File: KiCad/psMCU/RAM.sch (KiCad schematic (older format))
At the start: 26 parts

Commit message: Started work on schematic
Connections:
- net LATCHSAFEDA_EN/VAL renamed LED: LATCHSAFEDA_EN/VAL
- net R_ASYNC_SAFEA/VAL renamed LED: R_ASYNC_SAFEA/VAL
- net W_ASYNC/VAL renamed LED: W_ASYNC/VAL
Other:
- note added: "Latch Async Write.\nShould keep writes stable and \nprevent accidental writes."
- note added: "Only Do Something if RAM (0x000-0x0ff) and\nnot Periphs (0x100-0x1ff) are addressed."
- note removed: "Ensure Data is stabil during Write"
- note removed: "Only Do Something if RAM and\nnot Periphs are addressed."
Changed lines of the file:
@@
 $Descr A4 11693 8268
 encoding utf-8
-Sheet 51 65
+Sheet 21 94
 Title ""
 Date ""
@@
 Text HLabel 1050 1300 0    50   3State ~ 0
 DB[0..7]
-Text HLabel 1050 1650 0    50   Input ~ 0
+Text HLabel 1050 1650 0    50   BiDi ~ 0
 RAMA[0..8]
 Entry Wire Line
@@
 	1600 5900 1850 5900
 Text Notes 1550 6650 0    50   ~ 0
-Only Do Something if RAM and\nnot Periphs are addressed.
+Only Do Something if RAM (0x000-0x0ff) and\nnot Periphs (0x100-0x1ff) are addressed.
 Wire Bus Line
 	1950 1400 3800 1400
@@
 Wire Wire Line
 	4800 3000 4750 3000
-Text Notes 3950 3850 0    50   ~ 0
-Ensure Data is stabil during Write
+Text Notes 5050 4600 0    50   ~ 0
+Latch Async Write.\nShould keep writes stable and \nprevent accidental writes.
 Connection ~ 2750 3150
 Wire Wire Line
@@
 S 3100 5550 700  200
 U 5F31E1C9
-F0 "R_ASYNC_SAFEA" 50
+F0 "LED: R_ASYNC_SAFEA" 50
 F1 "1BitLED.sch" 50
 F2 "VAL" I L 3100 5650 50
@@
 S 3100 4650 700  200
 U 5F3261C9
-F0 "W_ASYNC" 50
+F0 "LED: W_ASYNC" 50
 F1 "1BitLED.sch" 50
 F2 "VAL" I L 3100 4750 50
@@
 S 3100 4050 700  200
 U 5F32E5C9
-F0 "LATCHSAFEDA_EN" 50
+F0 "LED: LATCHSAFEDA_EN" 50
 F1 "1BitLED.sch" 50
 F2 "VAL" I L 3100 4150 50

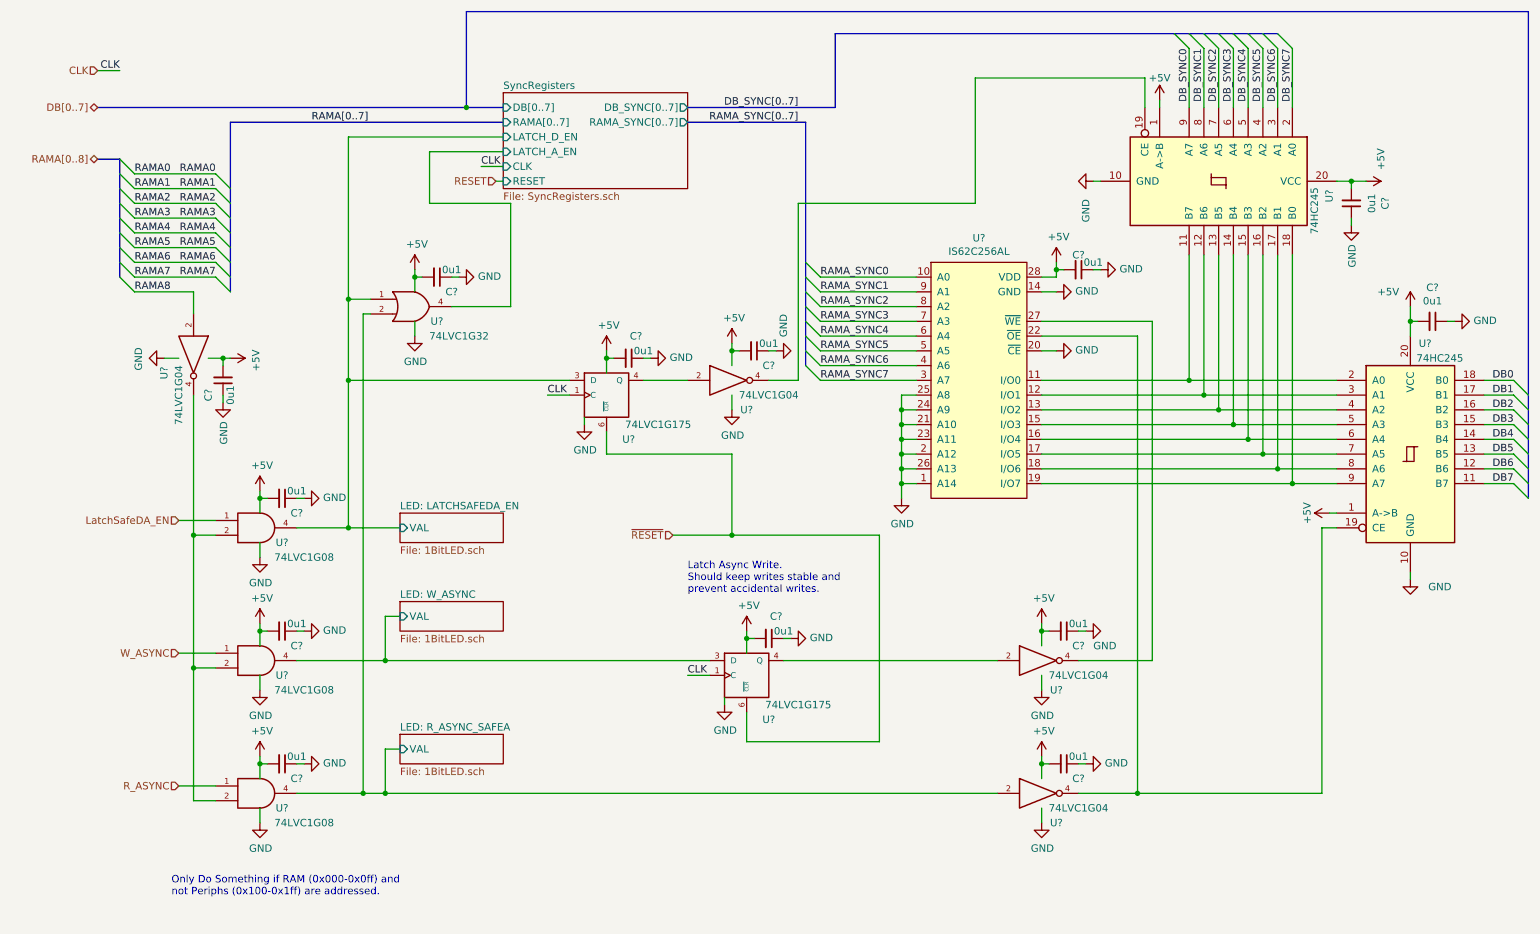
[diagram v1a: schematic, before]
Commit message: Started ClockTest PCB
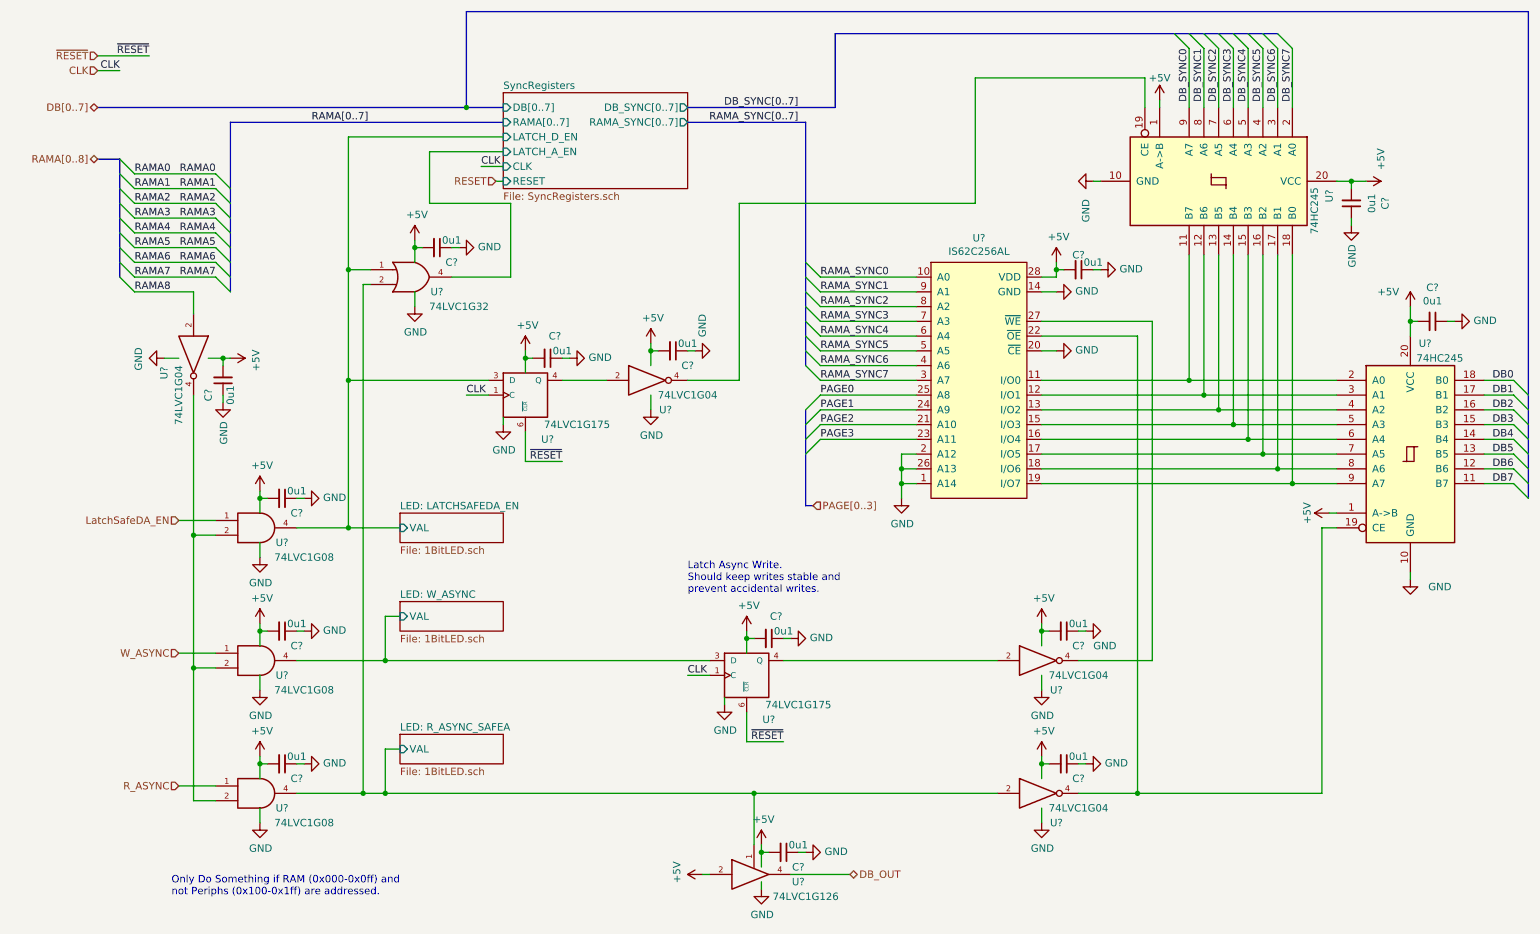
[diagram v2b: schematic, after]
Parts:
- added C?: 0u1, Capacitor_SMD:C_0603_1608Metric, symbol Device:C_Small
- added U?: 74LVC1G126, Package_TO_SOT_SMD:SOT-353_SC-70-5, symbol 74xGxx:74LVC1G126
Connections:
- net +5V: now also C?.2, U?.2, U?.5 (VCC)
- net GND: now also C?.1, U?.3 (GND); no longer U?.21 (A10), U?.23 (A11), U?.24 (A9), U?.25 (A8)
- net LED: R_ASYNC_SAFEA/VAL: now also U?.1
- new net DB_OUT: U?.4
- new net PAGE0: U?.25 (A8)
- new net PAGE1: U?.24 (A9)
- new net PAGE2: U?.21 (A10)
- new net PAGE3: U?.23 (A11)
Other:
- moved on the sheet: C?, U?

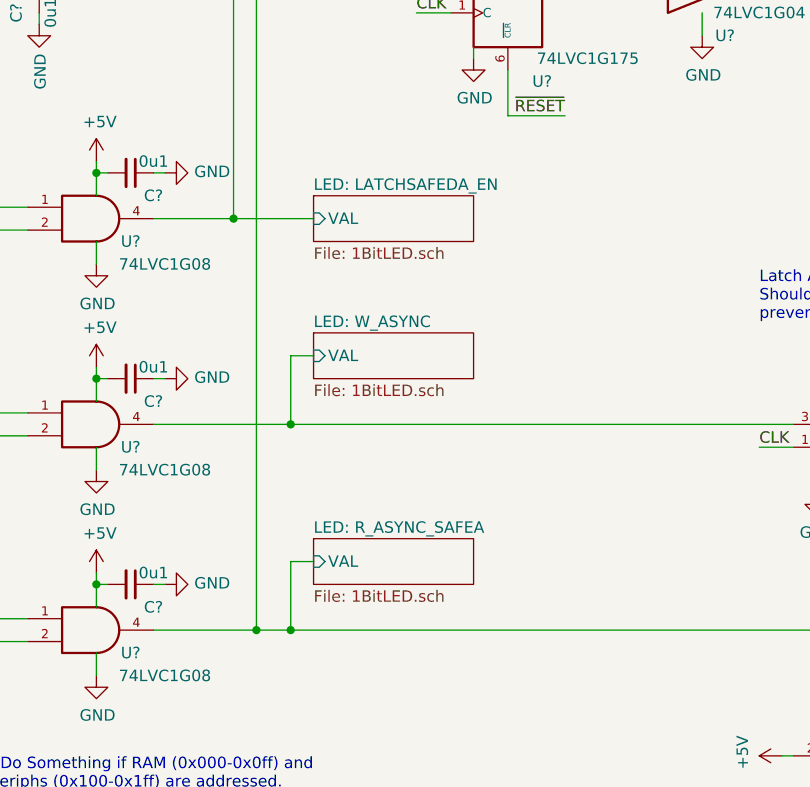
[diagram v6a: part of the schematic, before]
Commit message: Removed Single LED sheets
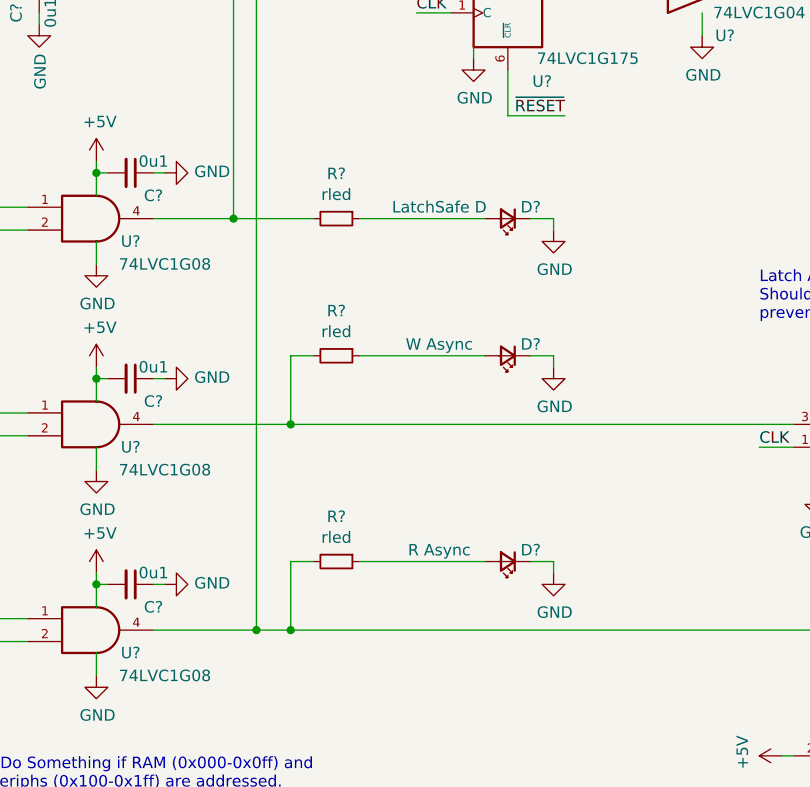
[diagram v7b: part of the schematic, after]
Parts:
- added D?: LatchSafe D, Diode_SMD:D_0603_1608Metric, symbol Device:LED_Small
- added D?: W Async, Diode_SMD:D_0603_1608Metric, symbol Device:LED_Small
- added D?: R Async, Diode_SMD:D_0603_1608Metric, symbol Device:LED_Small
- added R? (x3): rled, Resistor_SMD:R_0603_1608Metric, symbol Device:R_Small
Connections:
- net GND: now also D?.1 (K), D?.1 (K), D?.1 (K)
- net LED: LATCHSAFEDA_EN/VAL renamed SyncRegisters/LATCH_D_EN
- net SyncRegisters/LATCH_D_EN: now also R?.2
- net LED: R_ASYNC_SAFEA/VAL: no longer names the net of U?.1, U?.2, U?.2, U?.4
- net LED: R_ASYNC_SAFEA/VAL: now also R?.2
- net LED: W_ASYNC/VAL: no longer names the net of U?.3 (D), U?.4
- net LED: W_ASYNC/VAL: now also R?.2
- new net: D?.2 (A), R?.1 (x3)

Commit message: First Schematic Draft done.
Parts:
- C54, C55, C56, C57, C58, C59, C60, C61, C62, C63, C64, C65, C66, C67: renamed from C?; footprint Capacitor_SMD:C_0603_1608Metric -> NoRef_Footprints:C_0603_1608Metric_NoRef
- D48, D49, D50: renamed from D?; footprint Diode_SMD:D_0603_1608Metric -> NoRef_Footprints:D_0603_1608Metric_NoRef
- R50, R51, R52: renamed from R?; footprint Resistor_SMD:R_0603_1608Metric -> NoRef_Footprints:R_0603_1608Metric
- gave numbers to parts that had none: 14
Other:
- note added: "Latch Data and Adr. \nShould help prevent glitches."
